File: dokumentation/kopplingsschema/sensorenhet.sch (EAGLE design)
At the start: 3 parts, among them IC1 MEGA16-P

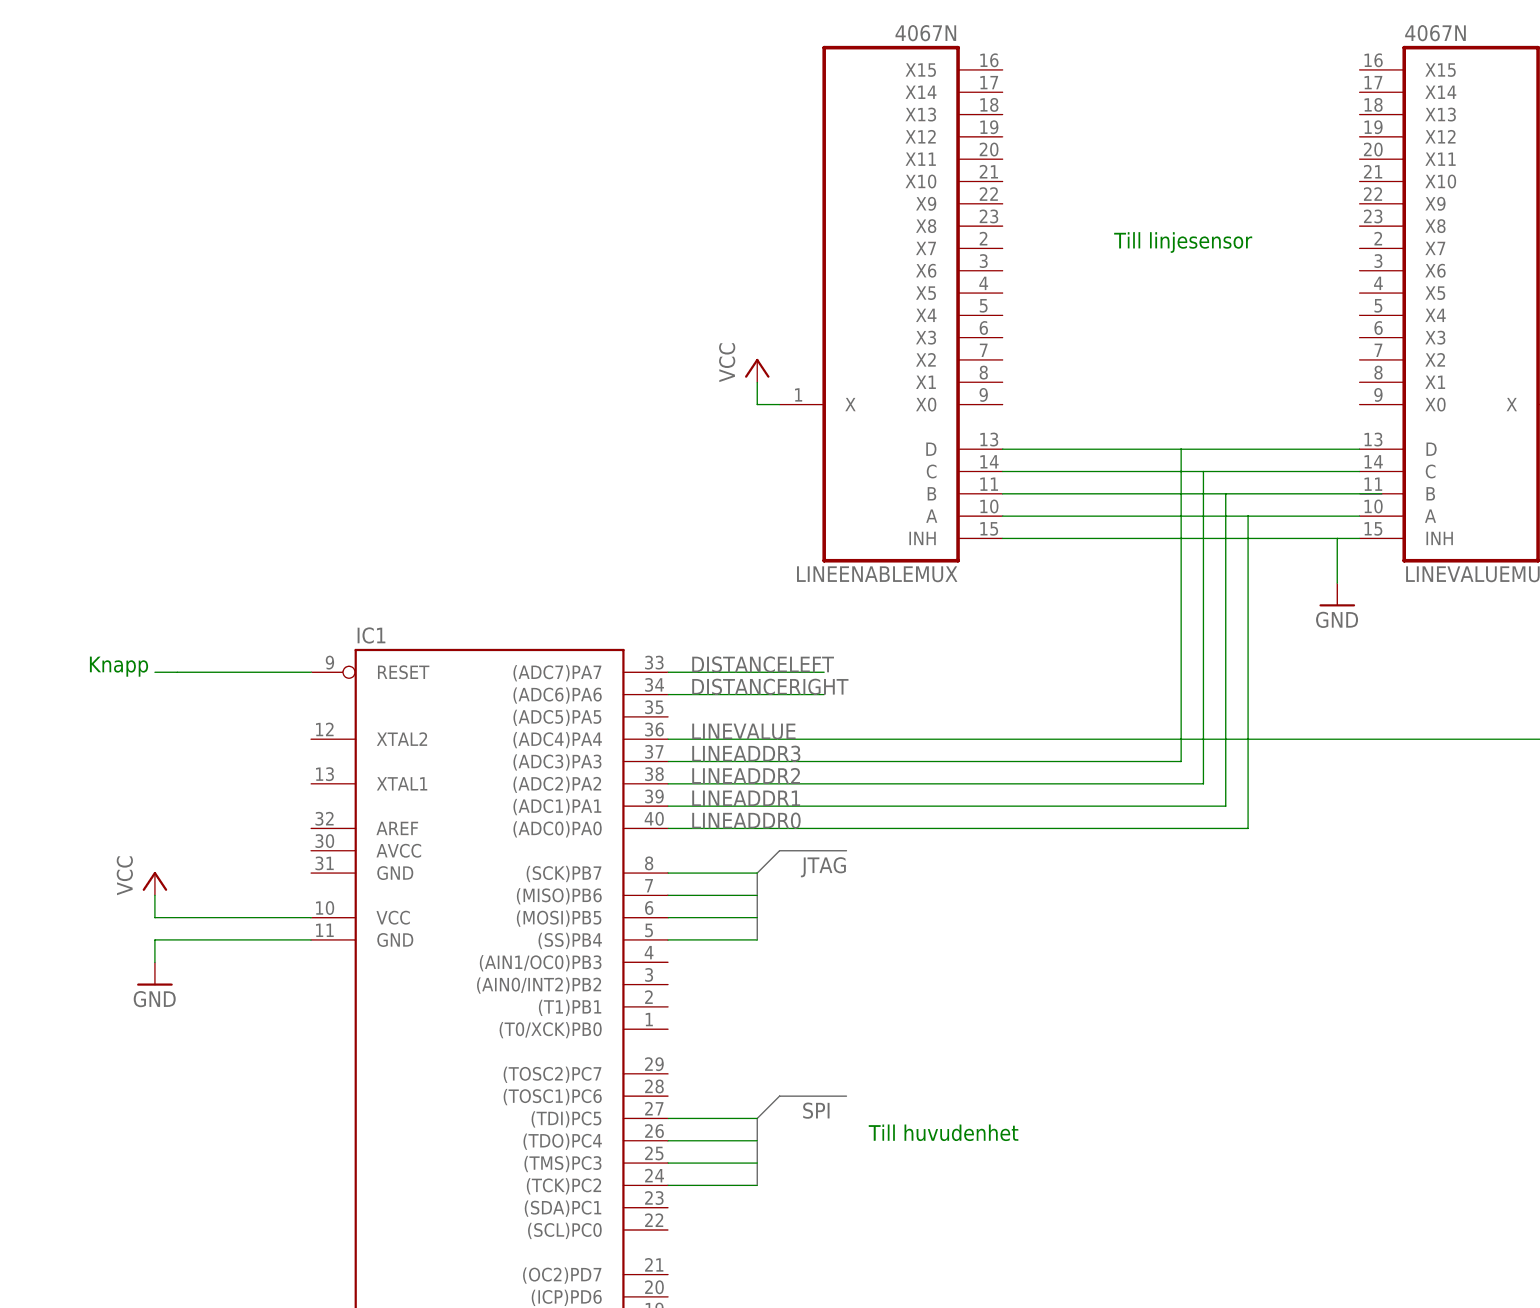
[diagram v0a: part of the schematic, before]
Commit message: Updated circuit diagrams.
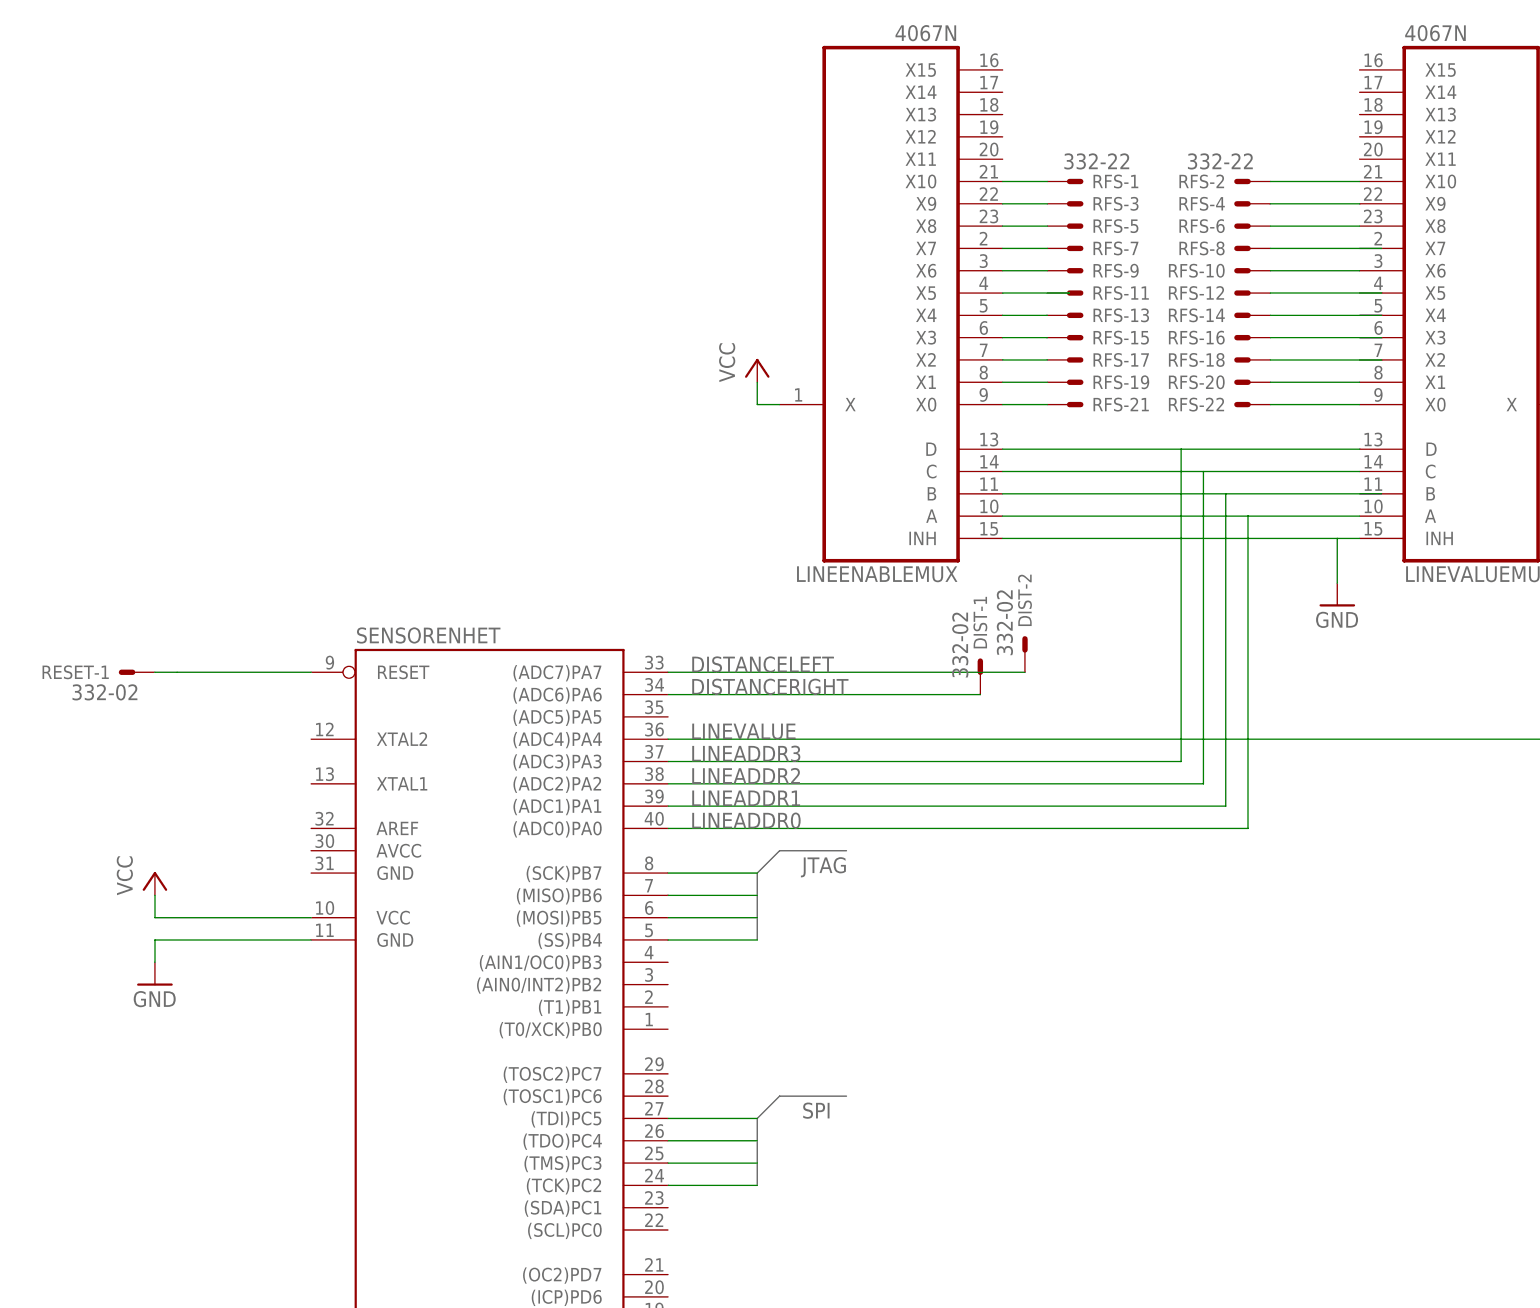
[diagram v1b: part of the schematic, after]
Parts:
- added DIST, RESET: 332-02, con-garry:332-02
- added RFS: 332-22, con-garry:332-22
- renumbered IC1 to SENSORENHET
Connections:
- new net N$10: LINEENABLEMUXA.X0, RFS-21.S
- new net N$11: LINEENABLEMUXA.X1, RFS-19.S
- new net N$12: LINEENABLEMUXA.X2, RFS-17.S
- new net N$13: LINEENABLEMUXA.X3, RFS-15.S
- new net N$14: LINEENABLEMUXA.X4, RFS-13.S
- new net N$15: LINEENABLEMUXA.X5
- new net N$16: LINEENABLEMUXA.X6, RFS-9.S
- new net N$17: LINEENABLEMUXA.X7, RFS-7.S
- new net N$18: LINEENABLEMUXA.X8, RFS-5.S
- new net N$19: LINEENABLEMUXA.X9, RFS-3.S
- new net N$20: LINEENABLEMUXA.X10, RFS-1.S
- new net N$21: LINEVALUEMUXA.X0, RFS-22.S
- new net N$22: LINEVALUEMUXA.X1, RFS-20.S
- new net N$23: RFS-18.S
- new net N$24: RFS-16.S
- new net N$25: RFS-14.S
- new net N$26: RFS-12.S
- new net N$27: LINEVALUEMUXA.X6, RFS-10.S
- new net N$28: RFS-8.S
- new net N$29: LINEVALUEMUXA.X8, RFS-6.S
- new net N$30: LINEVALUEMUXA.X9, RFS-4.S
- new net N$31: LINEVALUEMUXA.X10, RFS-2.S
- net N$5: now also RESET-1.S
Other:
- note removed: "Knapp"
- note removed: "Till huvudenhet"
- note removed: "Till linjesensor"

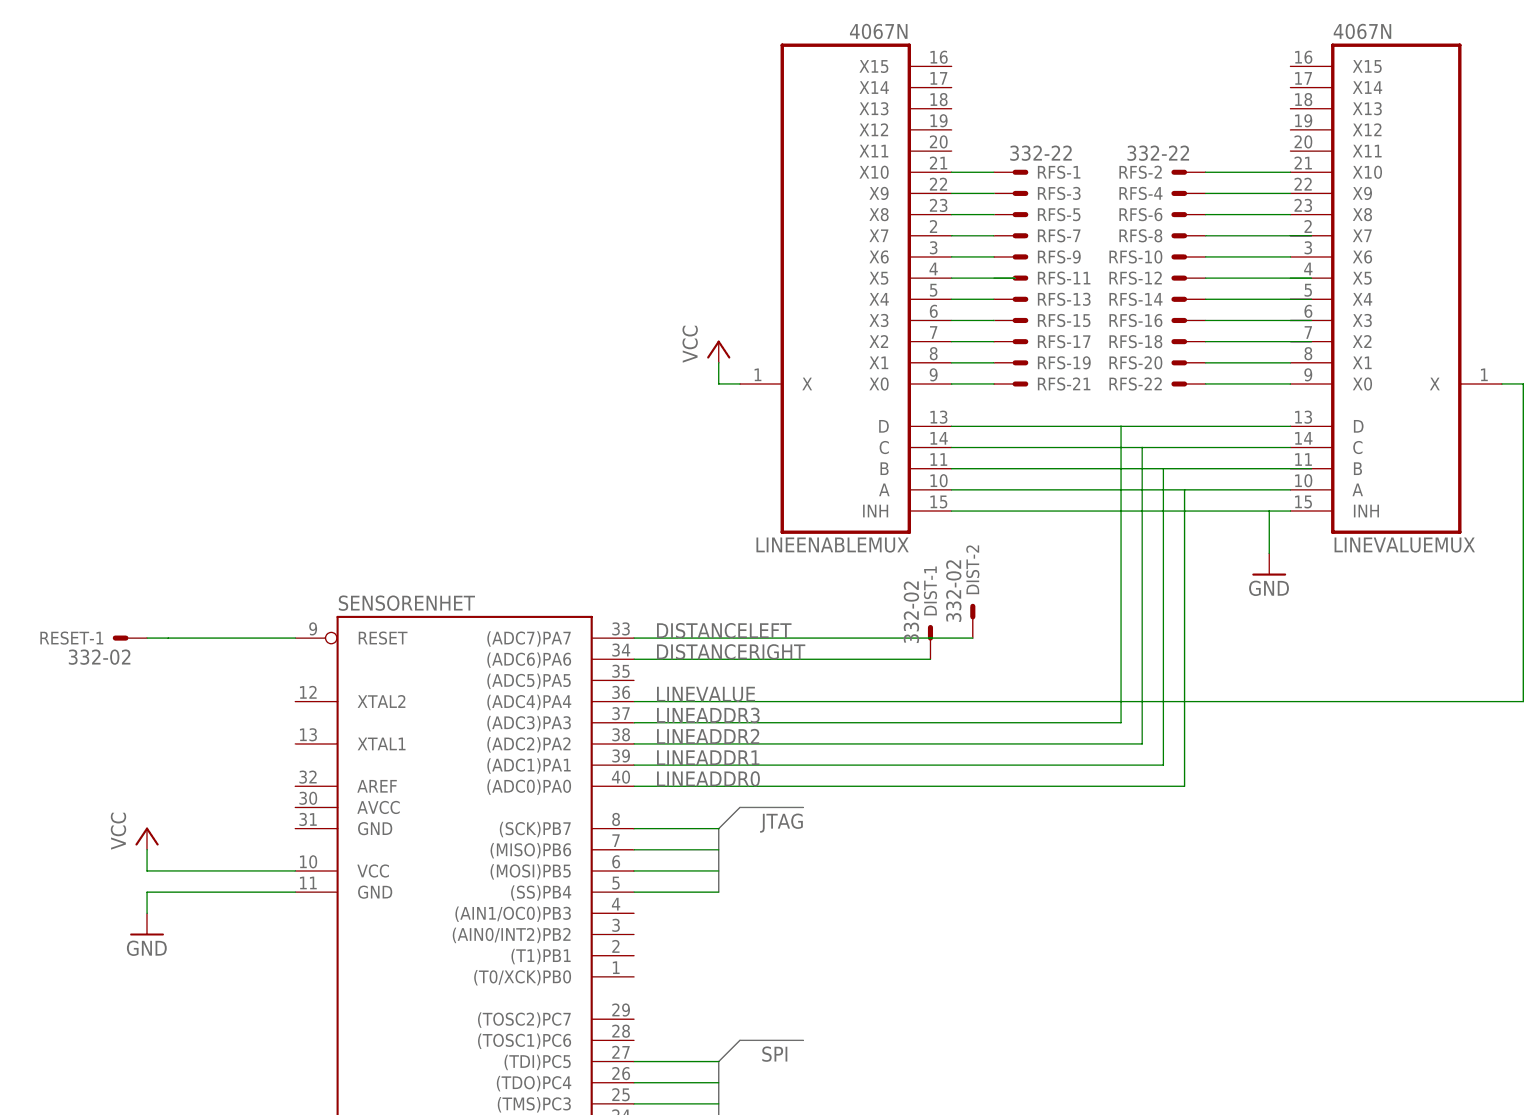
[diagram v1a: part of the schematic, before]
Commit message: Shrinked the circuit diagram.
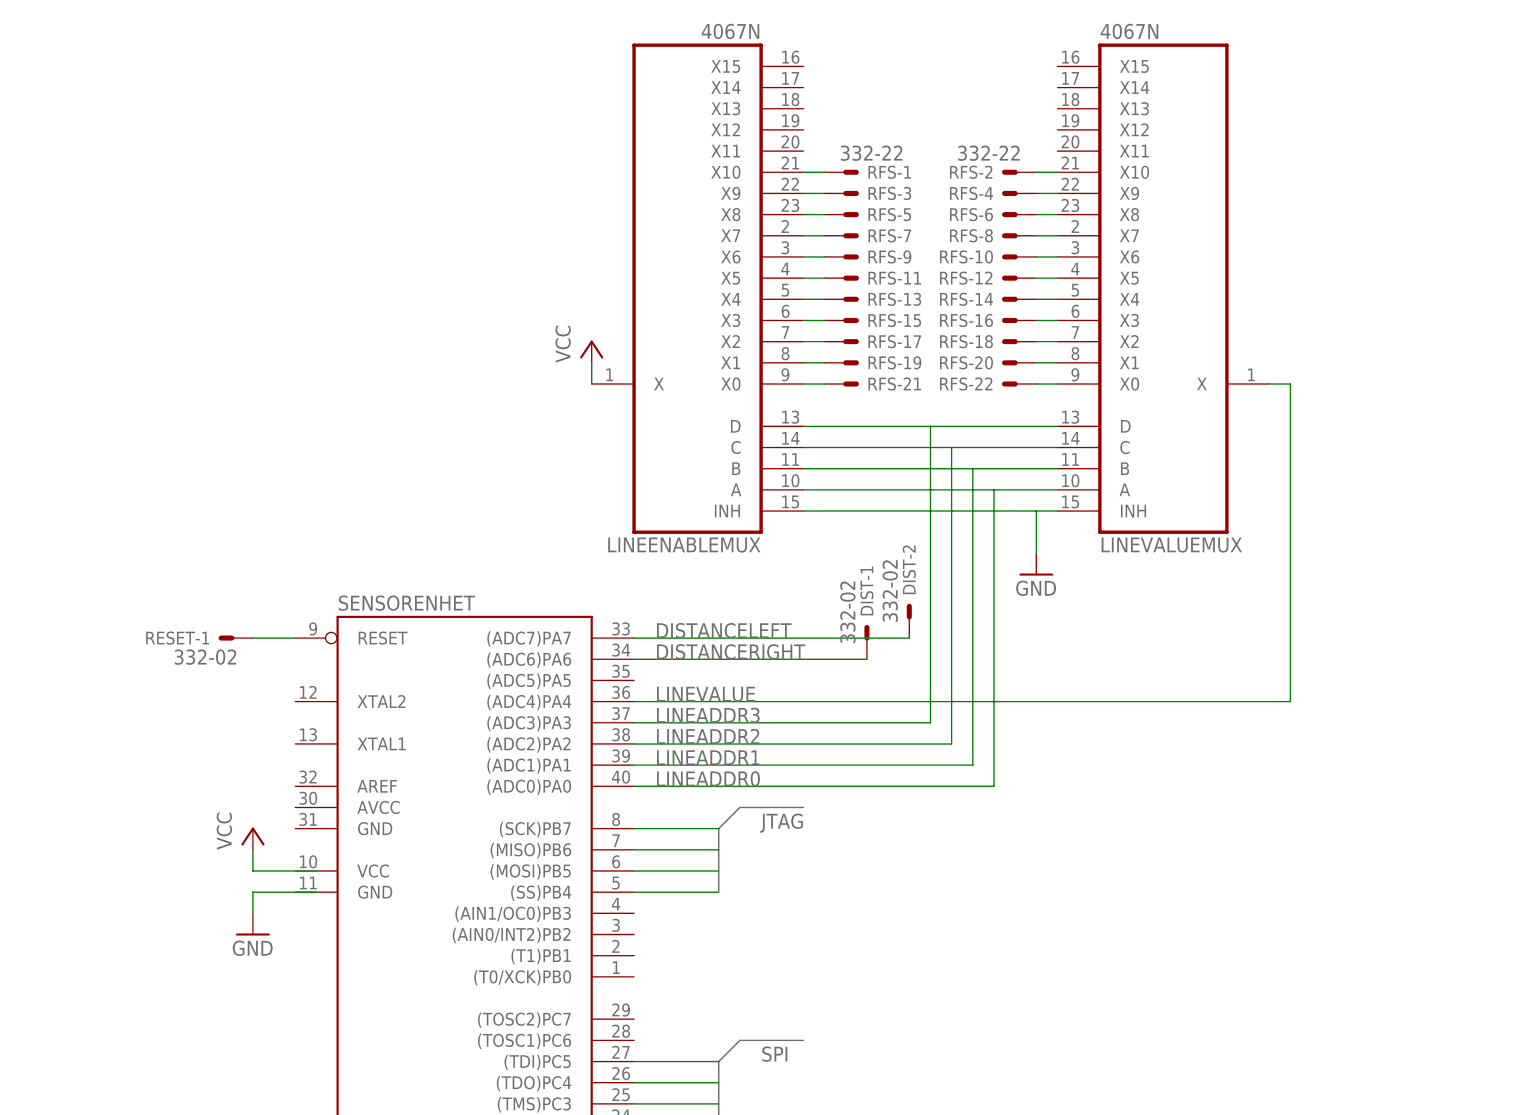
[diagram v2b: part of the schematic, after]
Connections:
- removed net N$23 (its old number): RFS-18.S
- removed net N$25 (its old number): RFS-14.S
- new net N$27: LINEVALUEMUXA.X4, RFS-14.S
- new net N$29: LINEVALUEMUXA.X2, RFS-18.S
- net DISTANCELEFT: now also DIST-2.S
- net DISTANCERIGHT: now also DIST-1.S
- net GND: no longer SENSORENHET.GND
- net LINEADDR1: now also LINEVALUEMUXA.B
- net N$15: now also RFS-11.S
- net N$24: now also LINEVALUEMUXA.X7, RFS-8.S; no longer RFS-16.S
- net N$26: now also LINEVALUEMUXA.X5
- net N$28: now also LINEVALUEMUXA.X3, RFS-16.S; no longer RFS-8.S
- net VCC: no longer SENSORENHET.VCC
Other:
- moved on the sheet: DIST-1, DIST-2, LINEENABLEMUX, LINEVALUEMUX, RESET-1, RFS-1, RFS-10, RFS-11, RFS-12, RFS-13, RFS-14, RFS-15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
